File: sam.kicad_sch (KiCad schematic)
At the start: 23 parts, among them IC4 74ACT02, IC5 74ACT138, IC6 74ACT138N, J1 JTAG, J3 Conn_01x24, J4 Conn_01x24, U3 XC95144XL-TQ100, X1 14.31818MHz

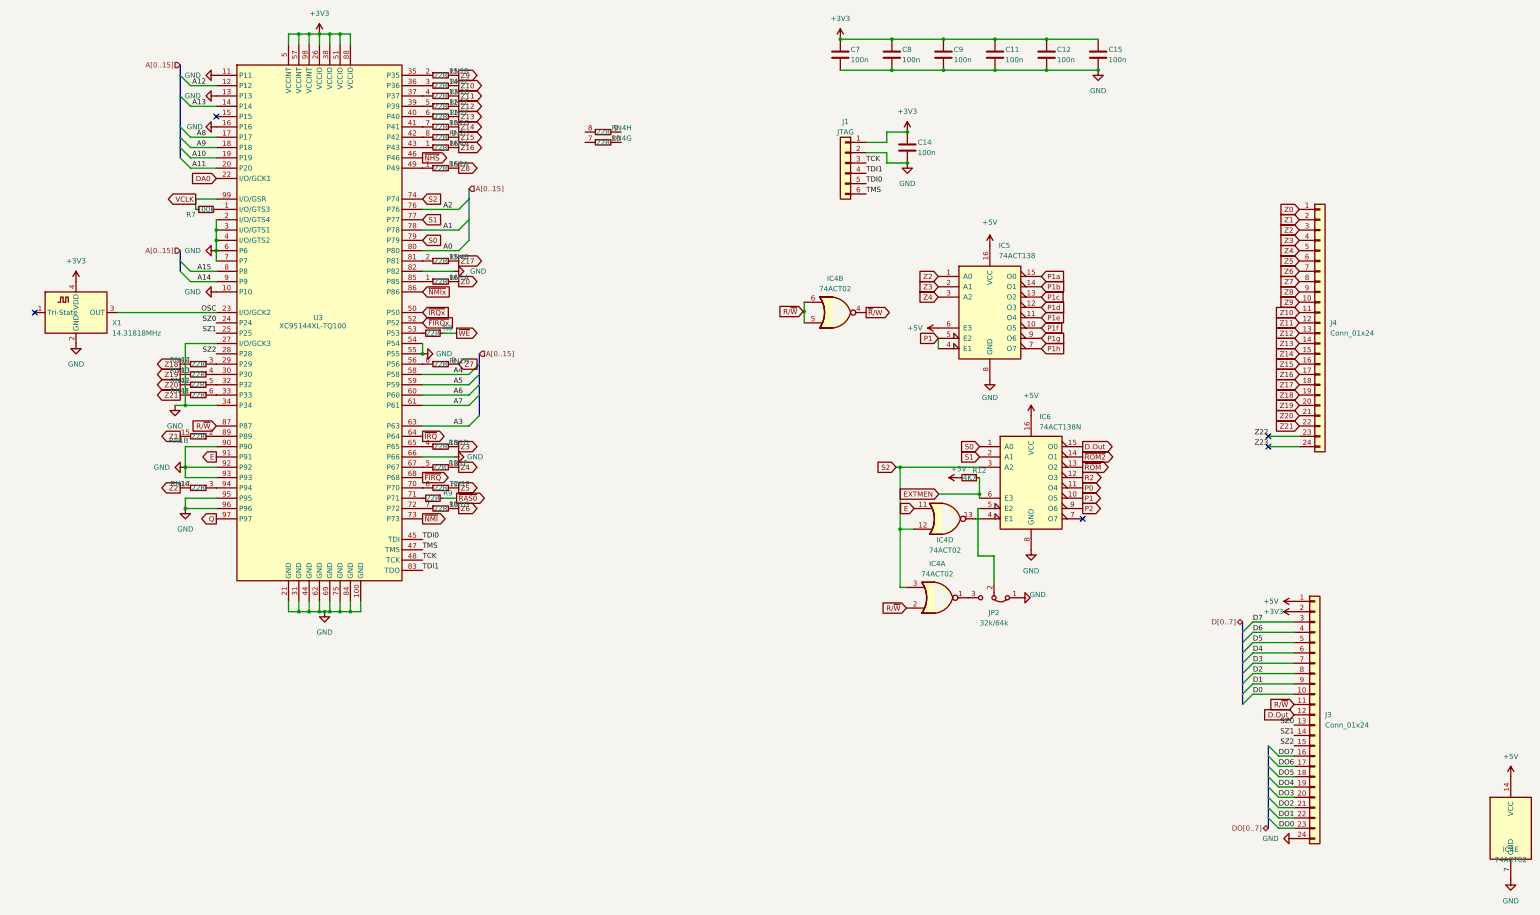
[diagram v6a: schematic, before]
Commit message: add data bus to sam schematic
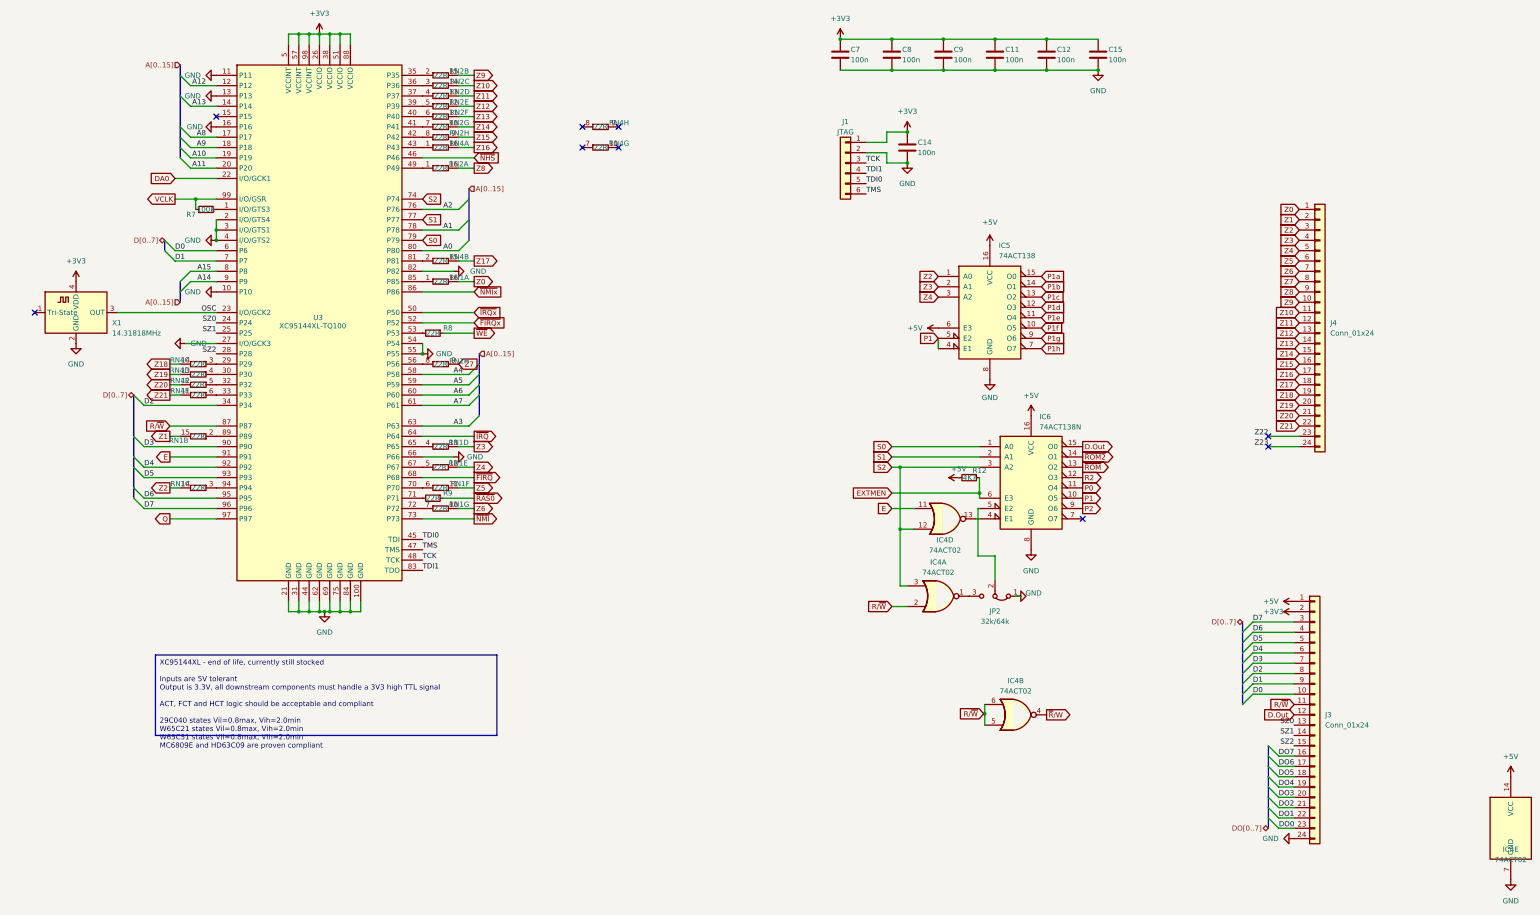
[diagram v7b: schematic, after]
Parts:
- IC6: SA2120 Sheet 1 -> (none)
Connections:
- net D0: now also U3.6 (P6)
- net D1: now also U3.7 (P7)
- net D2: now also U3.34 (P34)
- net D3: now also U3.90 (P90)
- net D4: now also U3.92 (P92)
- net D5: now also U3.93 (P93)
- net D6: now also U3.95 (P95)
- net D7: now also U3.96 (P96)
- net GND: no longer U3.34 (P34), U3.6 (P6), U3.7 (P7), U3.90 (P90), U3.92 (P92), U3.93 (P93), U3.95 (P95), U3.96 (P96)
- no-connect marks 5 -> 9
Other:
- moved on the sheet: IC4B, RN4G, RN4H

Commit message: route data bus to sam
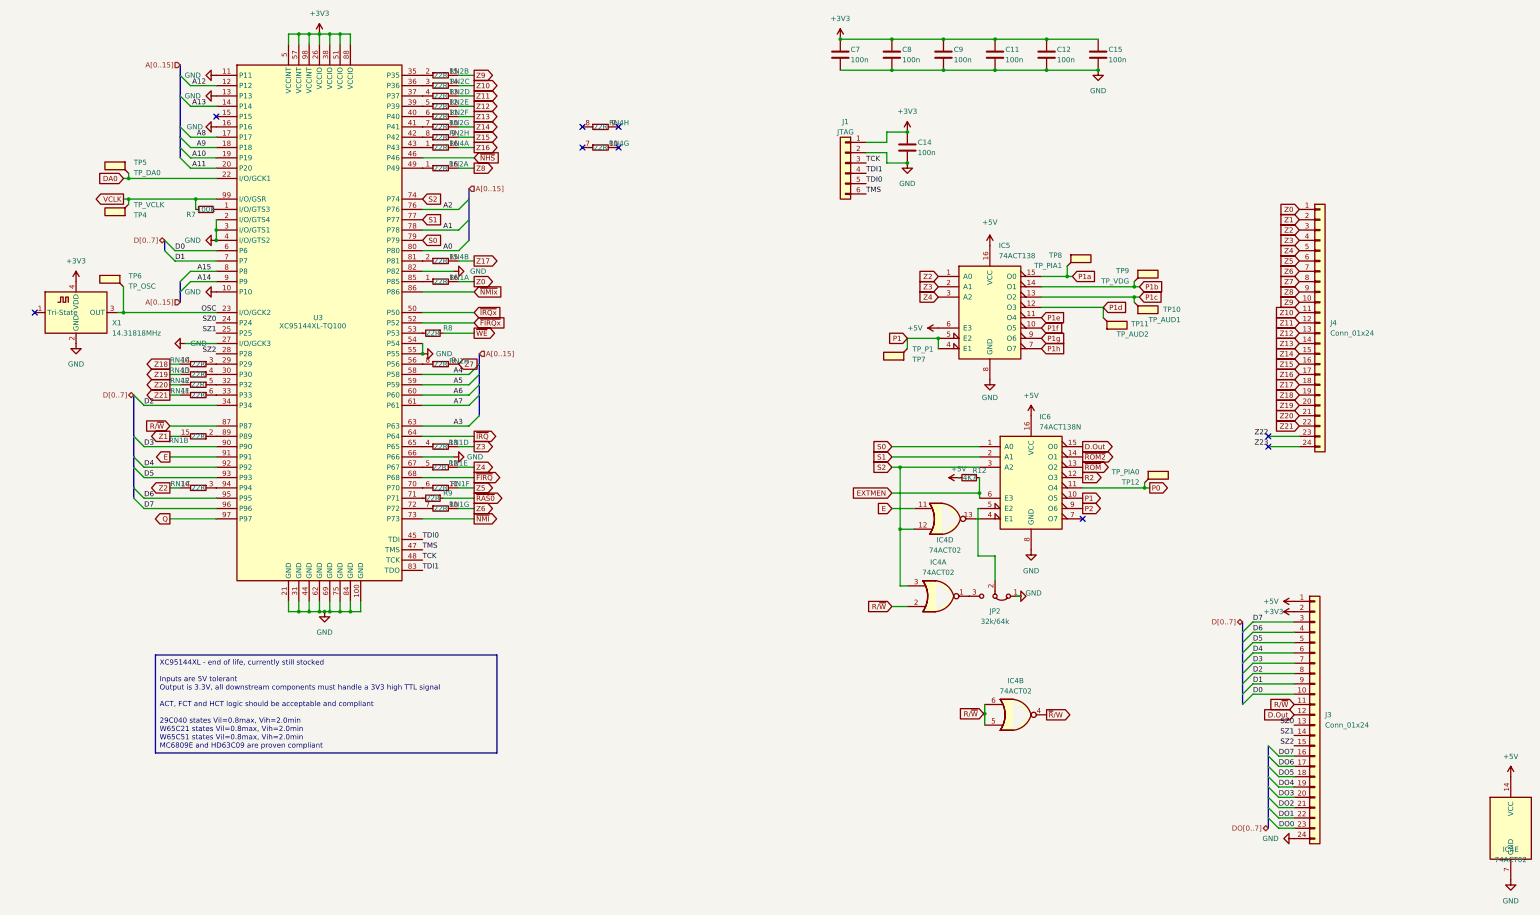
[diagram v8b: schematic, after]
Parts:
- added TP10: TP_AUD1, TestPoint:TestPoint_Loop_D1.80mm_Drill1.0mm_Beaded, symbol Connector:TestPoint_Flag
- added TP11: TP_AUD2, TestPoint:TestPoint_Loop_D1.80mm_Drill1.0mm_Beaded, symbol Connector:TestPoint_Flag
- added TP12: TP_PIA0, TestPoint:TestPoint_Loop_D1.80mm_Drill1.0mm_Beaded, symbol Connector:TestPoint_Flag
- added TP4: TP_VCLK, TestPoint:TestPoint_Loop_D1.80mm_Drill1.0mm_Beaded, symbol Connector:TestPoint_Flag
- added TP5: TP_DA0, TestPoint:TestPoint_Loop_D1.80mm_Drill1.0mm_Beaded, symbol Connector:TestPoint_Flag
- added TP6: TP_OSC, TestPoint:TestPoint_Loop_D1.80mm_Drill1.0mm_Beaded, symbol Connector:TestPoint_Flag
- added TP7: TP_P1, TestPoint:TestPoint_Loop_D1.80mm_Drill1.0mm_Beaded, symbol Connector:TestPoint_Flag
- added TP8: TP_PIA1, TestPoint:TestPoint_Loop_D1.80mm_Drill1.0mm_Beaded, symbol Connector:TestPoint_Flag
- added TP9: TP_VDG, TestPoint:TestPoint_Loop_D1.80mm_Drill1.0mm_Beaded, symbol Connector:TestPoint_Flag
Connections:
- net DA0: now also TP5.1
- net OSC: now also TP6.1
- net P0: now also TP12.1
- net P1: now also TP7.1
- net P1a: now also TP8.1
- net P1b: now also TP9.1
- net P1c: now also TP10.1
- net P1d: now also TP11.1
- net VCLK: now also TP4.1
